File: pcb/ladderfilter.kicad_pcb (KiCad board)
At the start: 2 copper layers, 98 x 100 mm, 67 parts, among them J10 v/oct, J11 CV, J3 Eurorack power, J6 header main, J8 audio in, J9 audio out, Q1 BC547C, Q10 BC547C, Q11 BC547C, Q12 BC557C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

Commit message: convert to new format
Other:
- net class Default removed

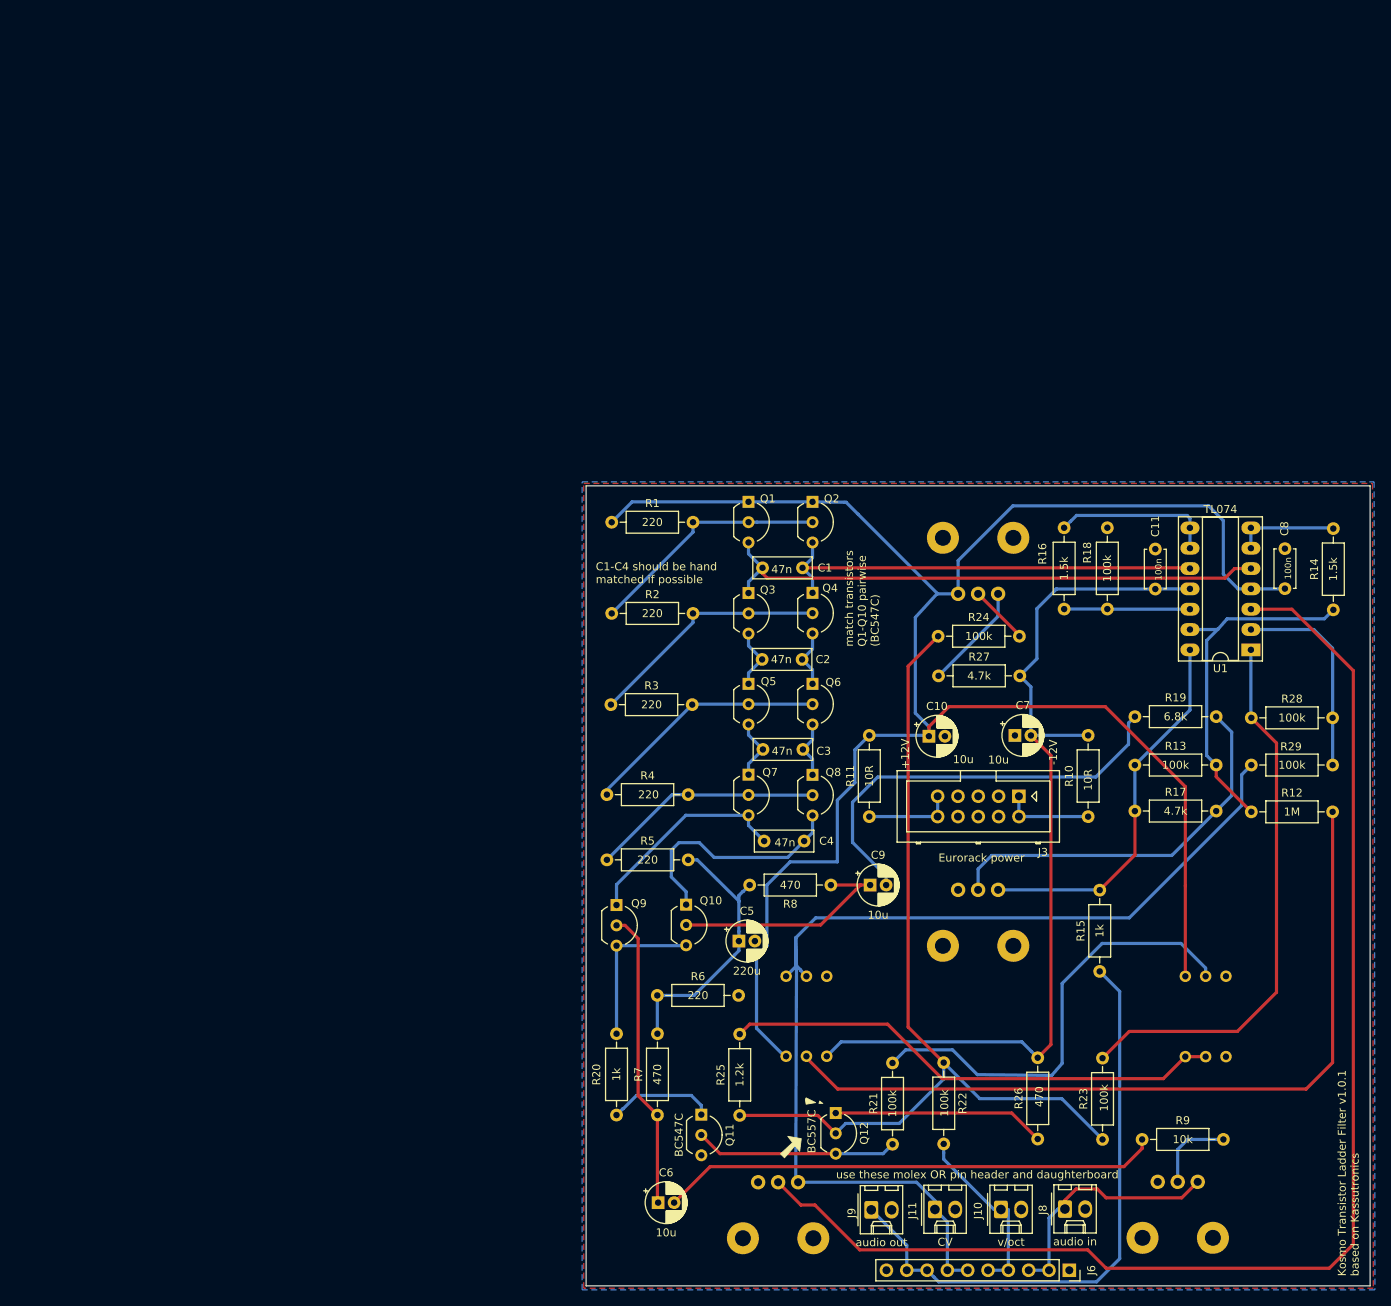
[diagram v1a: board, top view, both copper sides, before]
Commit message: lay out transistor ladder
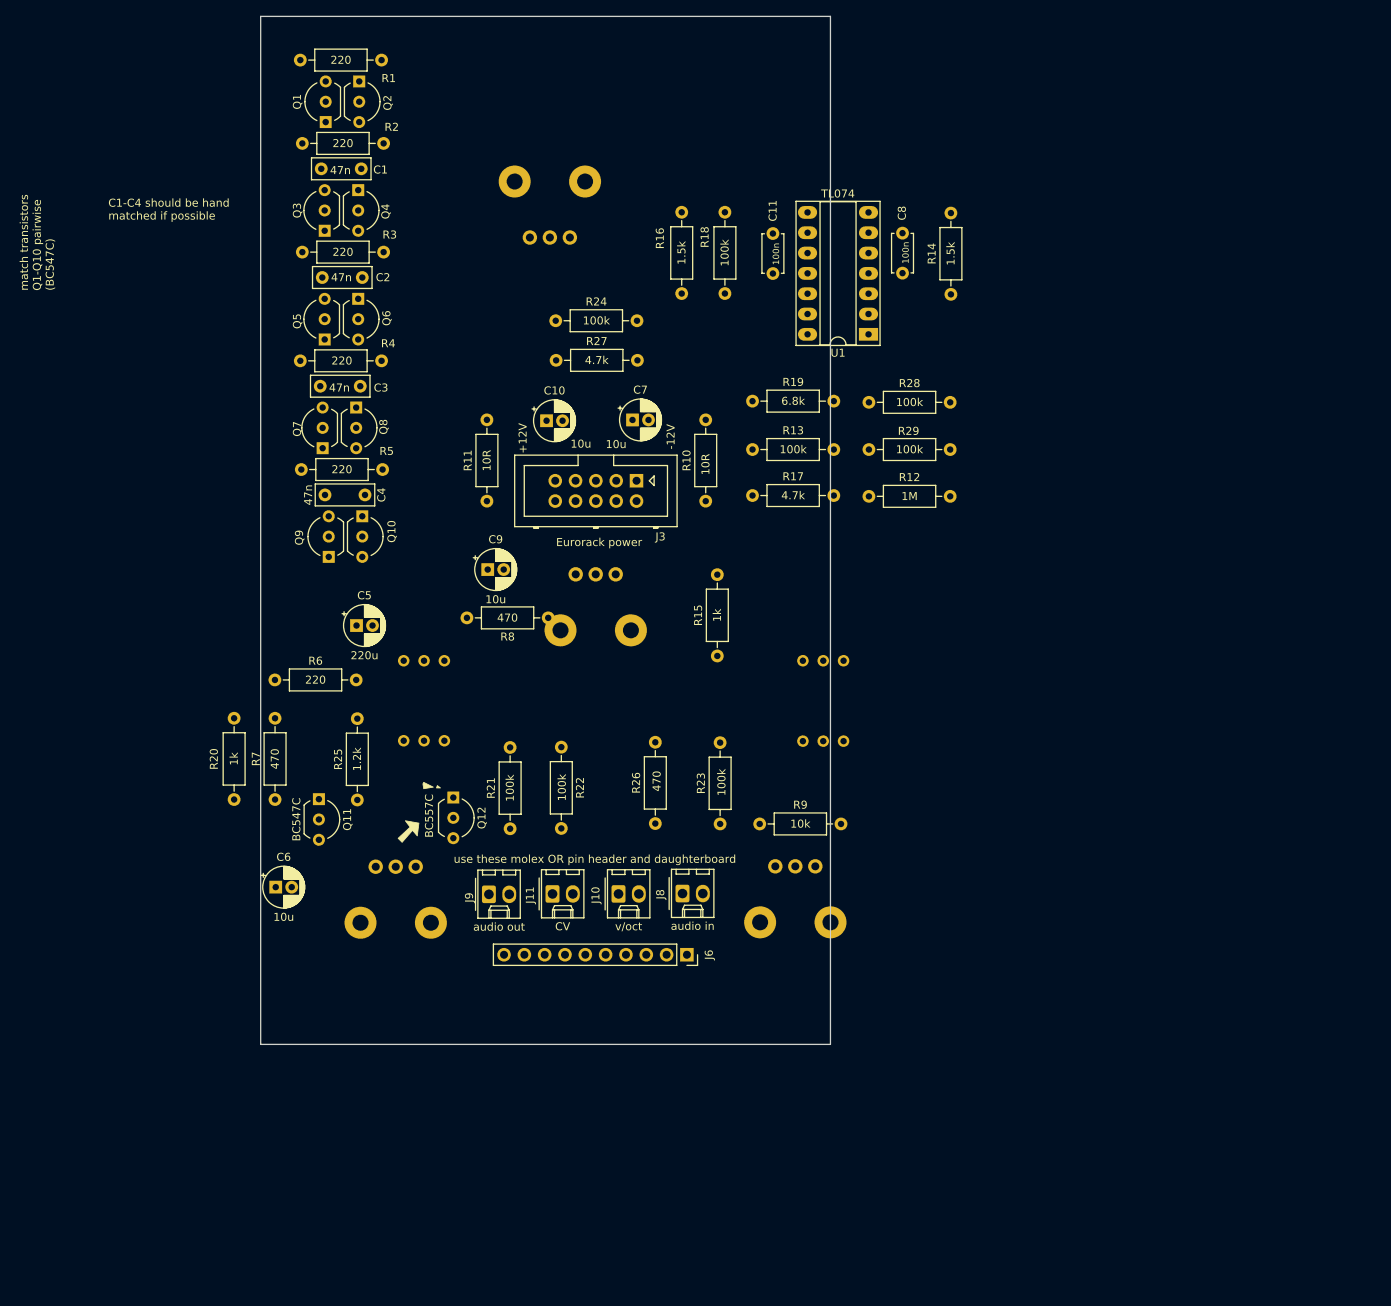
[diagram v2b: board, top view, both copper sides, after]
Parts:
- moved Q2 77.3 mm to (32.6, 28.4)
- moved Q4 75.9 mm to (32.5, 42.0)
- moved Q6 74.4 mm to (32.5, 55.6)
- moved C1 74.4 mm to (32.9, 39.4)
- moved Q8 73.2 mm to (32.3, 69.2)
- moved C2 72.8 mm to (33.0, 53.0)
- moved C3 71.6 mm to (32.8, 66.5)
- moved Q1 71.0 mm to (28.4, 33.5), turned to 90 degrees
- moved R2 70.3 mm to (25.5, 36.2)
- moved C4 69.9 mm to (33.4, 80.1)
- moved Q3 69.7 mm to (28.3, 47.1), turned to 90 degrees
- moved R1 69.7 mm to (25.3, 25.8)
- moved RV5 69.6 mm to (54.0, 48.0)
- moved R3 68.5 mm to (25.5, 49.8)
- moved Q5 68.3 mm to (28.3, 60.7), turned to 90 degrees
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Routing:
- net +12V: track 245.4 -> 0.00 mm
- net Net-(RV8-Pad2): track 165.3 -> 0.00 mm
- net MAIN_CV: track 135.9 -> 0.00 mm
- net -12V: track 114.8 -> 0.00 mm
- net Net-(Q12-Pad2): track 111.8 -> 0.00 mm
- net Net-(R12-Pad2): track 100.2 -> 0.00 mm
- net MAIN_AUDIO_OUT: track 74.7 -> 0.00 mm
- net OUT_L: track 70.3 -> 0.00 mm
- net CV_IN_2: track 69.3 -> 0.00 mm
- net Net-(R25-Pad2): track 62.7 -> 0.00 mm
- net Net-(C6-Pad2): track 62.4 -> 0.00 mm
- net Net-(R21-Pad2): track 56.2 -> 0.00 mm
- net OUT_R: track 55.8 -> 0.00 mm
- net Net-(C9-Pad2): track 53.4 -> 0.00 mm
- net Net-(R17-Pad2): track 48.8 -> 0.00 mm
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- removed copper zone on B.Cu, net GND
- removed copper zone on F.Cu, net GND
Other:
- board size 98 x 100 mm -> 71.2 x 128.5 mm
- board text removed: "Kosmo Transistor Ladder Filter v1.0.1 based on Kassutronics"
